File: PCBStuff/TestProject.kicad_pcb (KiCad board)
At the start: 2 copper layers, 66 x 30.5 mm, 6 parts, among them J1_Barrel1 Barrel_Jack, J2_XT60 Barrel_Jack, J3_Buck1 Conn_01x03_Female, J4_LED1 Conn_01x03_Female, J5_MCU_Left1 Conn_01x07_Female, J5_MCU_Right1 Conn_01x07_Female

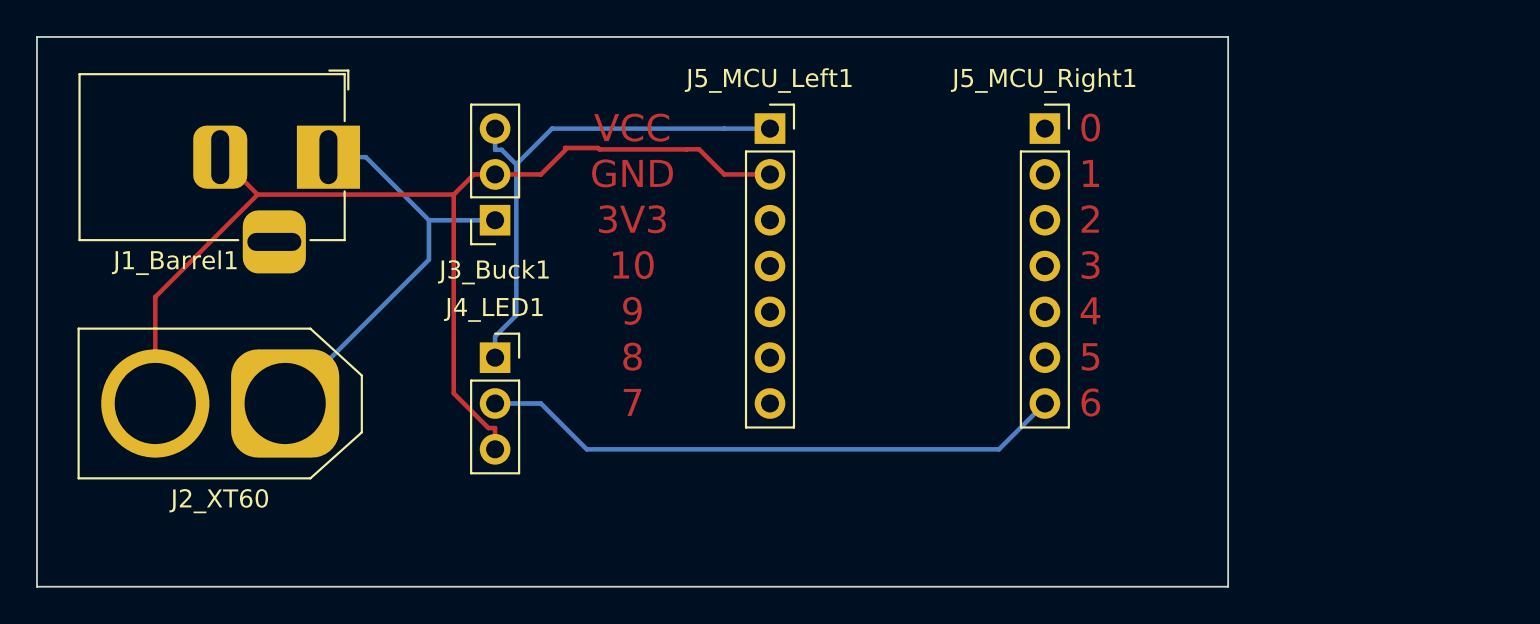
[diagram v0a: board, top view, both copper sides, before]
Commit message: Made a first draft for EBoard
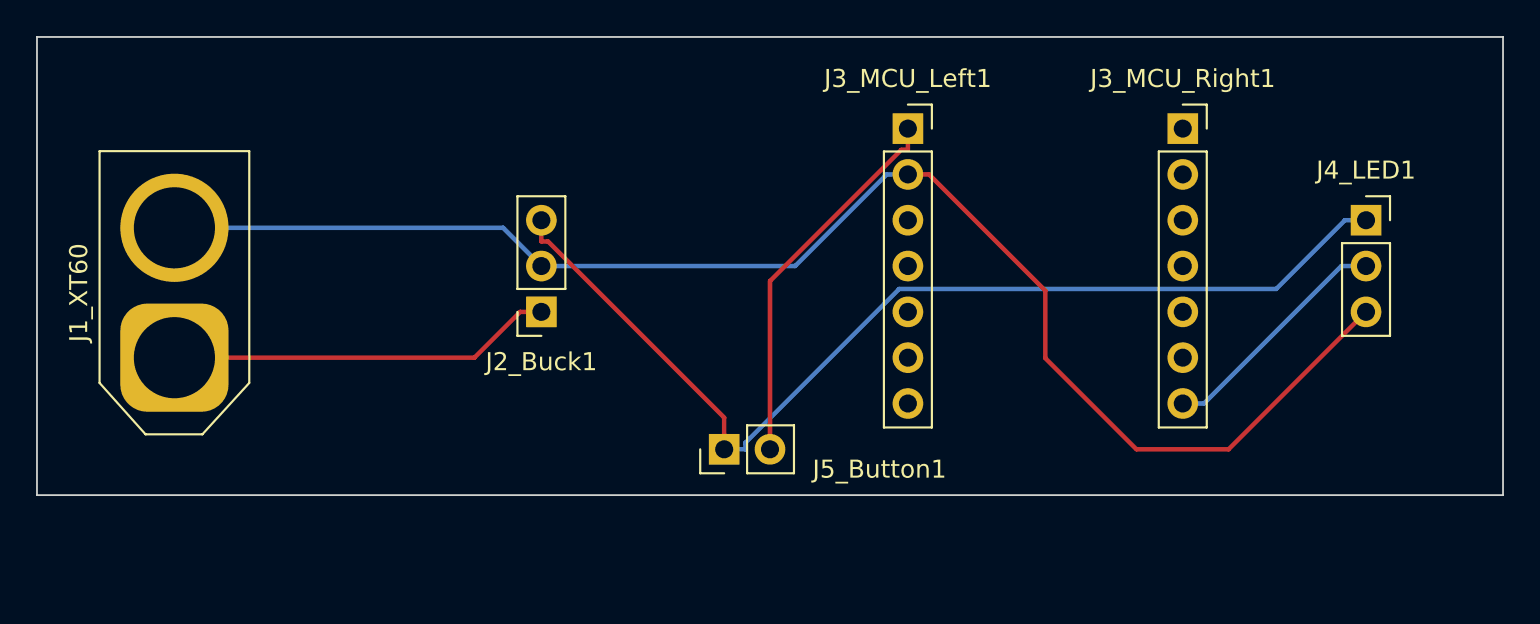
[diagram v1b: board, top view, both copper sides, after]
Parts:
- removed J1_Barrel1: Barrel_Jack, Connector_BarrelJack:BarrelJack_Horizontal
- removed J2_XT60: Barrel_Jack, Connector_AMASS:AMASS_XT60-M_1x02_P7.20mm_Vertical
- removed J3_Buck1: Conn_01x03_Female, Connector_PinSocket_2.54mm:PinSocket_1x03_P2.54mm_Vertical
- removed J5_MCU_Left1, J5_MCU_Right1: Conn_01x07_Female, Connector_PinSocket_2.54mm:PinSocket_1x07_P2.54mm_Vertical
- added J1_XT60: Conn_01x02_Male, Connector_AMASS:AMASS_XT60-M_1x02_P7.20mm_Vertical, F.Cu at (20.3, 30.5)
- added J2_Buck1: Conn_01x03_Female, Connector_PinSocket_2.54mm:PinSocket_1x03_P2.54mm_Vertical, F.Cu at (40.7, 27.9)
- added J3_MCU_Left1: Conn_01x07_Female, Connector_PinSocket_2.54mm:PinSocket_1x07_P2.54mm_Vertical, F.Cu at (61.0, 17.8)
- added J3_MCU_Right1: Conn_01x07_Female, Connector_PinSocket_2.54mm:PinSocket_1x07_P2.54mm_Vertical, F.Cu at (76.2, 17.8)
- added J5_Button1: Conn_01x02_Male, Connector_PinHeader_2.54mm:PinHeader_1x02_P2.54mm_Vertical, F.Cu at (50.8, 35.6)
- J4_LED1: value Conn_01x03_Female -> Conn_01x03_Male
- moved J4_LED1 48.9 mm to (86.4, 22.9)
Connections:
- J4_LED1 pad 1: V_5 -> V5
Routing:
- net V5: track 0.00 -> 58.2 mm
- net V_5: track 28.8 -> 0.00 mm
- net V_batt: track 24.2 -> 0.00 mm
- net Vin: track 0.00 -> 21.4 mm
- net ButtonOut: track 0.00 -> 21.2 mm
- net SIG_LED: track 32.6 -> 13.3 mm
- net GND: track 62.3 -> 80.7 mm
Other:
- board size 66 x 30.5 mm -> 81.3 x 25.4 mm
- board text added: "V_In"
- board text added: "V_Out"
- board text removed: "0"
- board text removed: "1"
- board text removed: "10"
- board text removed: "2"
- board text removed: "3"
- board text removed: "3V3"
- board text removed: "4"
- board text removed: "5"
- board text removed: "6"
- board text removed: "7"
- board text removed: "8"
- board text removed: "9"
- board text removed: "VCC"

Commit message: Made new gerbers including drillfile to make holes in jlcpcb
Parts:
- moved J2_Buck1 5.08 mm to (40.7, 22.9), turned to 0 degrees
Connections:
- J1_XT60 pad 1: Vin -> GND
- J1_XT60 pad 2: GND -> Vin
- J4_LED1 pad 1: V5 -> ButtonOut
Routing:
- net V5: track 58.2 -> 13.3 mm
- net ButtonOut: track 21.2 -> 50.0 mm
- net GND: track 80.7 -> 73.4 mm
- net Vin: track 21.4 -> 20.5 mm
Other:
- board text added: "+"
- board text added: "-"
- board text added: "EBoard v1.0.0"
- board text added: "Vin"
- board text added: "Vout"
- board text removed: "V_In"
- board text removed: "V_Out"

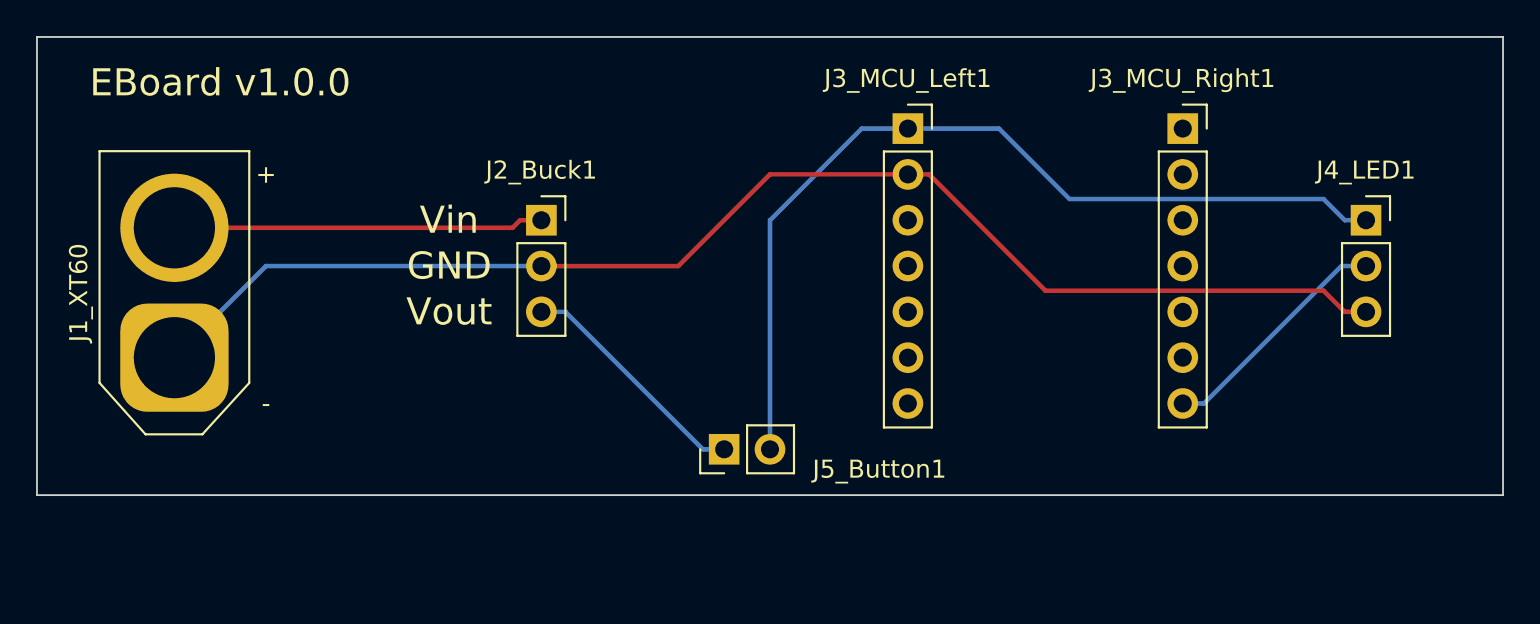
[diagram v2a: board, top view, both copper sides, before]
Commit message: Fixed footprint of MCU, re-organized header layout to shrink overall boardsize
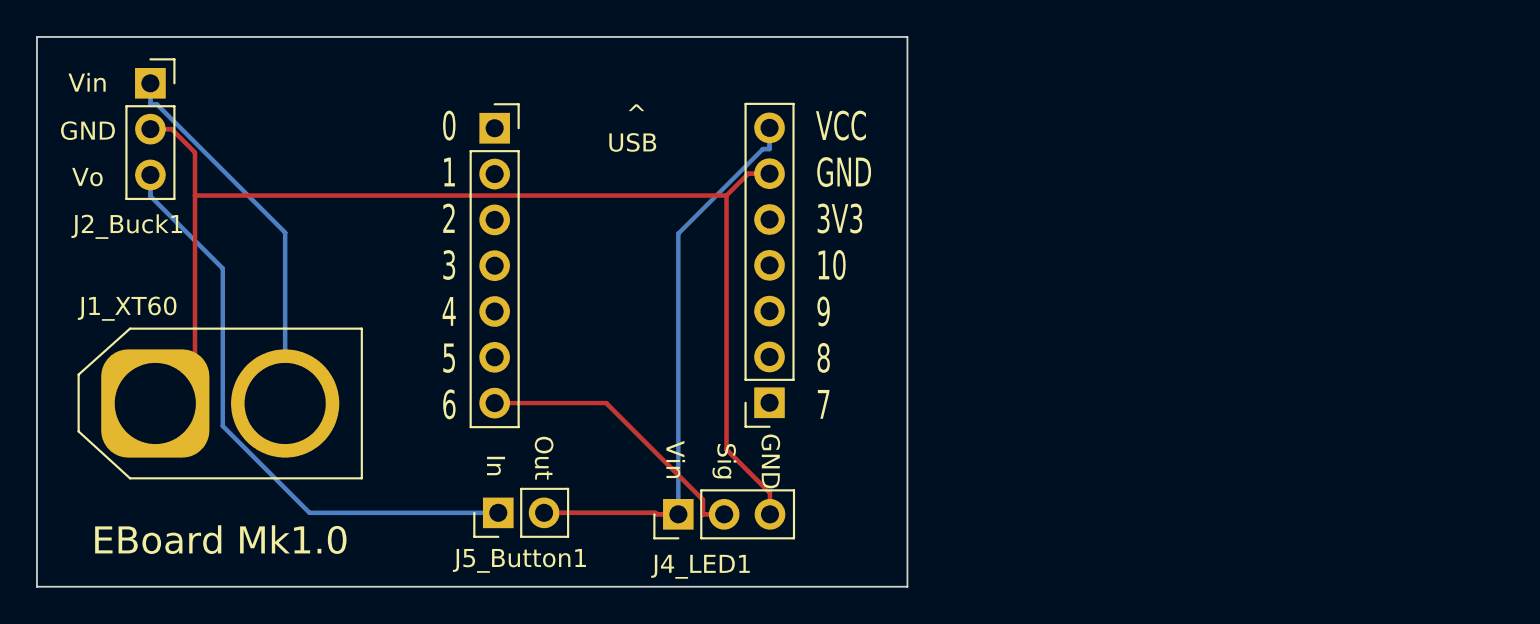
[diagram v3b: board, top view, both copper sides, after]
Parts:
- J4_LED1: footprint Connector_PinSocket_2.54mm:PinSocket_1x03_P2.54mm_Vertical -> Connector_PinHeader_2.54mm:PinHeader_1x03_P2.54mm_Vertical
- moved J4_LED1 41.5 mm to (48.3, 39.2), turned to 90 degrees
- moved J3_MCU_Left1 38.2 mm to (38.1, 17.8)
- moved J2_Buck1 23.0 mm to (19.0, 15.3)
- moved J3_MCU_Right1 17.0 mm to (53.3, 33.0), turned to 180 degrees
- moved J5_Button1 13.0 mm to (38.3, 39.1)
- moved J1_XT60 2.75 mm to (19.3, 33.0), turned to 0 degrees
- renumbered J3_MCU_Right1 to J3_MCU_Left1, J3_MCU_Left1 to J3_MCU_Right1
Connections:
- J3_MCU_Right1 pad 1: ButtonOut -> unconnected-(J3_MCU_Right1-Pad1)
- J3_MCU_Right1 pad 2: GND -> unconnected-(J3_MCU_Right1-Pad2)
- J3_MCU_Right1 pad 6: unconnected-(J3_MCU_Left1-Pad6) (its old number) -> GND
- J3_MCU_Right1 pad 7: unconnected-(J3_MCU_Left1-Pad7) -> ButtonOut
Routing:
- net V5: track 13.3 -> 32.9 mm
- net ButtonOut: track 50.0 -> 31.2 mm
- net GND: track 73.4 -> 68.9 mm
- net SIG_LED: track 13.3 -> 15.8 mm
- net Vin: track 20.5 -> 21.1 mm
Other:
- board size 81.3 x 25.4 mm -> 48.3 x 30.5 mm
- board text added: "0 1 2 3 4 5 6"
- board text added: "EBoard Mk1.0"
- board text added: "In"
- board text added: "Out"
- board text added: "Sig"
- board text added: "VCC GND 3V3 10 9 8 7"
- board text added: "Vo"
- board text added: "^ USB"
- board text removed: "+"
- board text removed: "-"
- board text removed: "EBoard v1.0.0"
- board text removed: "Vout"
